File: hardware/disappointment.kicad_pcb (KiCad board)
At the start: 2 copper layers, 175.3 x 58.4 mm, 56 parts, among them J1 Bus_ISA_16bit, J3 Conn_02x10_Odd_Even, J5 ATX-24, U1 F85226AF

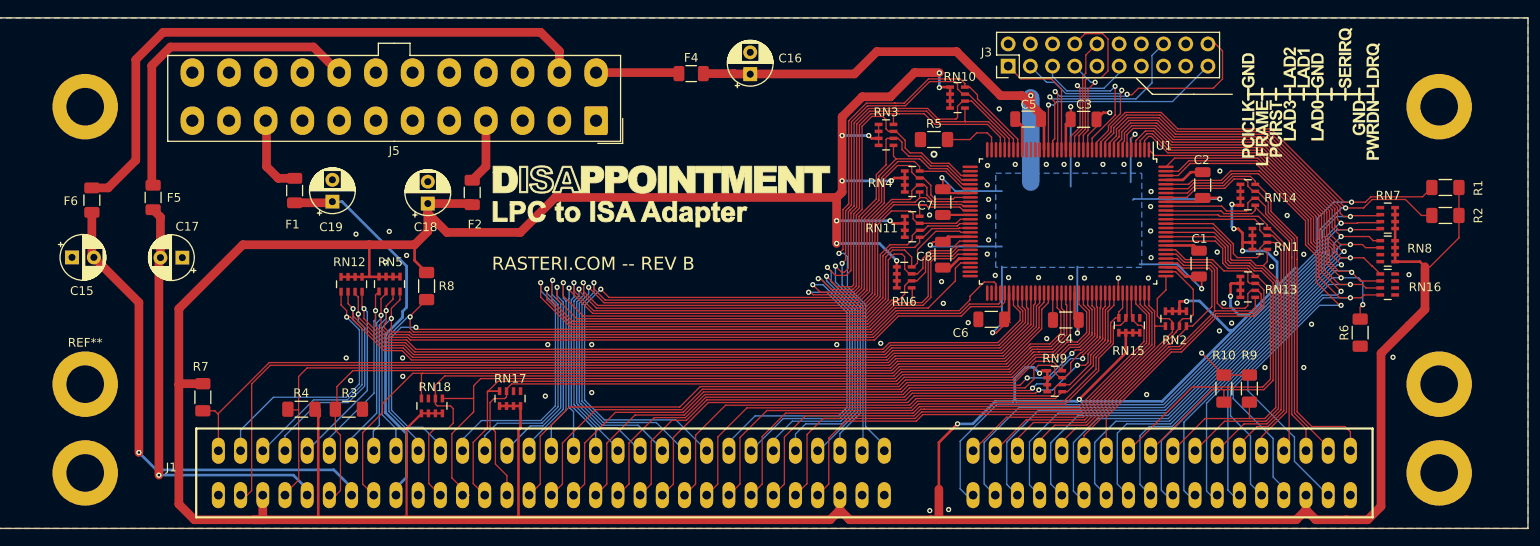
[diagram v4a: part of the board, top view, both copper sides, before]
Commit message: LEDs, -5v regulator
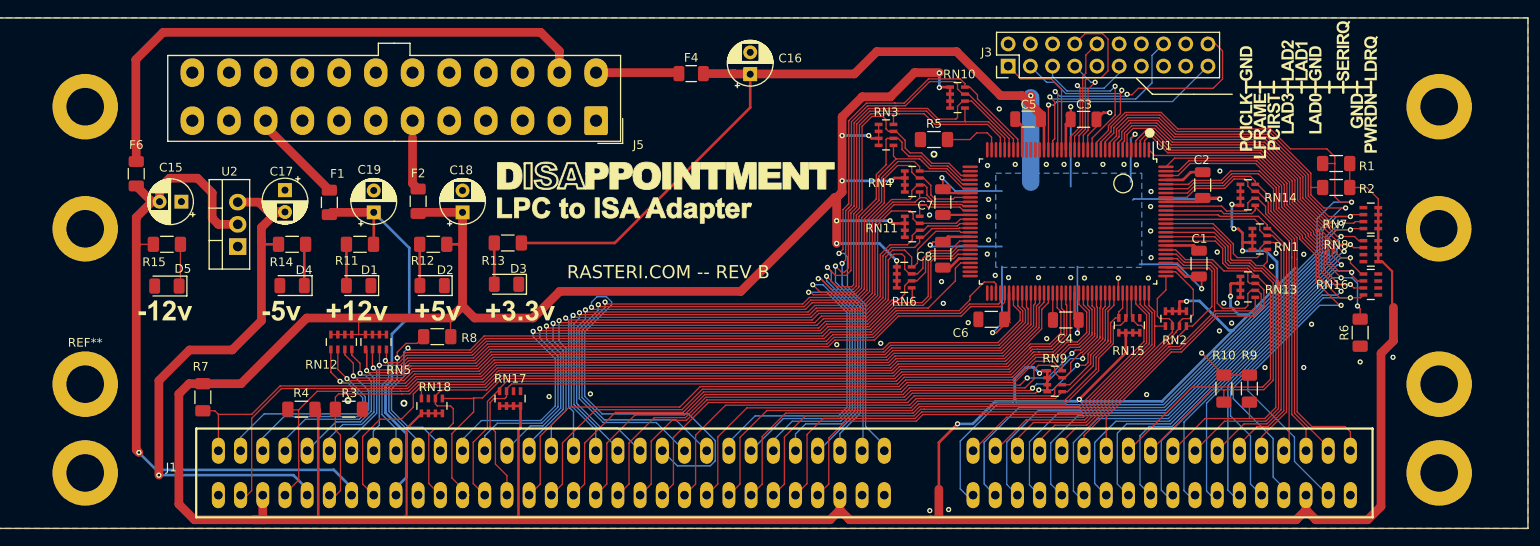
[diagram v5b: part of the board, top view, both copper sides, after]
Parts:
- removed F5: Polyfuse, Fuse:Fuse_1206_3216Metric
- added ?: , , F.Cu at (224.0, 120.5)
- added ?: , , F.Cu at (69.2, 103.7)
- added D1: LED, LED_SMD:LED_1206_3216Metric, F.Cu at (100.5, 110.2)
- added D2: LED, LED_SMD:LED_1206_3216Metric, F.Cu at (108.9, 110.2)
- added D3: LED, LED_SMD:LED_1206_3216Metric, F.Cu at (117.4, 110.1)
- added D4: LED, LED_SMD:LED_1206_3216Metric, F.Cu at (92.8, 110.2)
- added D5: LED, LED_SMD:LED_1206_3216Metric, F.Cu at (78.5, 110.3)
- added R11: 1K, Resistor_SMD:R_1206_3216Metric_Pad1.30x1.75mm_HandSolder, F.Cu at (100.6, 105.5)
- added R12: 1K, Resistor_SMD:R_1206_3216Metric_Pad1.30x1.75mm_HandSolder, F.Cu at (109.0, 105.5)
- added R13: 1K, Resistor_SMD:R_1206_3216Metric_Pad1.30x1.75mm_HandSolder, F.Cu at (117.5, 105.3)
- added R14: 1K, Resistor_SMD:R_1206_3216Metric_Pad1.30x1.75mm_HandSolder, F.Cu at (92.8, 105.5)
- added R15: 1K, Resistor_SMD:R_1206_3216Metric_Pad1.30x1.75mm_HandSolder, F.Cu at (78.5, 105.5)
- added U2: L7905, Package_TO_SOT_THT:TO-220-3_Vertical, F.Cu at (86.6, 105.7)
- F1, F2, F4, F6: value Polyfuse -> 500mA
- moved C17 14.1 mm to (92.0, 99.3), turned to -90 degrees
- moved C15 14.0 mm to (80.2, 100.6), turned to 180 degrees
- moved R2 12.9 mm to (212.3, 99.0)
- moved R1 12.8 mm to (212.3, 96.2)
- moved RN5 6.81 mm to (102.4, 116.7)
- moved RN12 6.71 mm to (98.5, 116.7)
- moved F2 6.27 mm to (107.3, 100.6)
- moved R8 5.92 mm to (109.4, 116.1), turned to 0 degrees
- moved F6 5.91 mm to (75.0, 97.4)
- moved C19 4.89 mm to (102.2, 101.8)
- moved F1 4.20 mm to (97.1, 100.7)
- moved C18 4.10 mm to (112.3, 101.8)
- moved RN16 1.93 mm to (216.3, 110.1)
- moved RN7 1.93 mm to (216.3, 102.5)
- moved RN8 1.93 mm to (216.3, 106.3)
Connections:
- ? pad 1: (no net) -> GND (x5)
- J5 pad 20: Net-(J5--5V) -> unconnected-(J5--5V-Pad20)
- REF** pad 1: (no net) -> GND
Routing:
- net Net-(J5--5V): track 37.3 -> 0.00 mm
- net +3.3V: track 165.7 -> 202.1 mm
- net -12V: track 56.6 -> 76.7 mm
- net -5V: track 50.5 -> 67.3 mm
- net /SA10: track 81.9 -> 97.6 mm
- net +5V: track 572.4 -> 562.7 mm
- net /IOCS16#: track 106.0 -> 97.8 mm
- net /SD1: track 94.9 -> 87.1 mm
- net /SA17: track 84.7 -> 77.1 mm
- net /SA19: track 88.4 -> 81.4 mm
- net /SA18: track 82.3 -> 75.6 mm
- net /SD2: track 96.1 -> 89.6 mm
- net /SD0: track 94.4 -> 88.0 mm
- net Net-(J5--12V): track 71.0 -> 64.8 mm
- net /MEMCS16#: track 111.1 -> 105.3 mm
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
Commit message: pson
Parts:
- added J2: Conn_01x02_Pin, Connector_PinHeader_2.54mm:PinHeader_1x02_P2.54mm_Vertical, F.Cu at (137.7, 91.9)
- added R16: 4.7K, Resistor_SMD:R_1206_3216Metric_Pad1.30x1.75mm_HandSolder, F.Cu at (168.0, 82.8)
- moved D5 7.16 mm to (85.7, 110.3)
- moved ? 3.81 mm to (213.9, 85.9)
- moved ? 3.81 mm to (69.2, 85.9)
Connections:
- J5 pad 16: unconnected-(J5-PS_ON#-Pad16) -> Net-(J2-Pin_1)
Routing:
- net Net-(J2-Pin_1): track 0.00 -> 26.2 mm
- net /PWRDN#: track 25.2 -> 39.0 mm
- net +3.3V: track 202.1 -> 210.8 mm
- net GND: track 30.0 -> 36.2 mm, vias 56 -> 63
- net Net-(D5-K): track 4.84 -> 9.82 mm
- net +5V: track 562.7 -> 561.3 mm
- net /SD4: track 99.4 -> 100.4 mm
- net /SD5: track 103.5 -> 104.2 mm
- net /IRQ9: track 104.5 -> 105.1 mm
- net Net-(J5--12V): track 64.8 -> 64.2 mm
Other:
- board text added: "PS_ON"
- board text added: "RASTERI.COM -- v0.2"
- board text removed: "RASTERI.COM -- REV B"
